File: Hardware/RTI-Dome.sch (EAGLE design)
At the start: 48 parts, among them IC1 24AA128ST, IC2 74LVC244, IC3 FT232RL, IC4 74ABT244, X13 PN61729-S

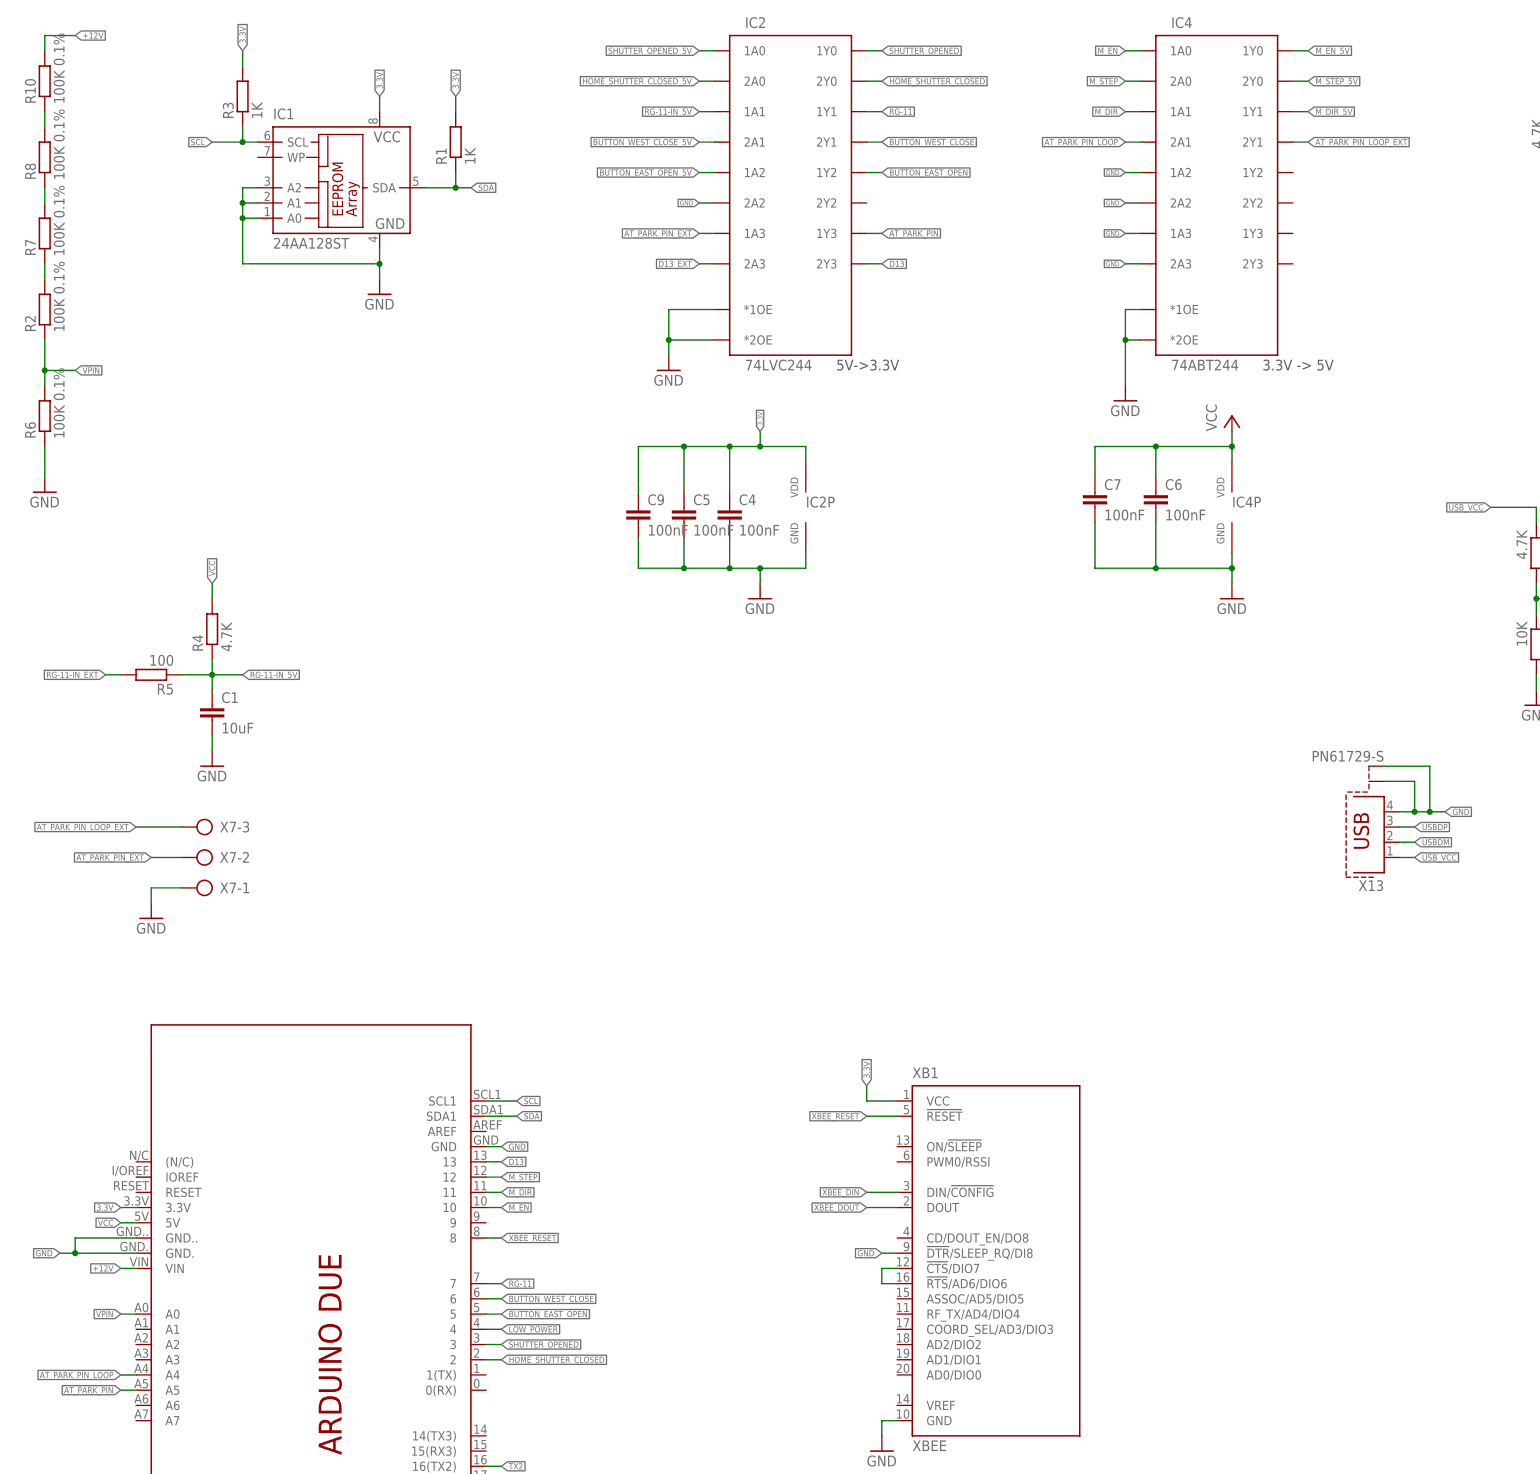
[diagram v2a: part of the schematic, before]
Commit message: Re-did the board with 74xx245 buffers instead of 244. Easier to route. Added a png to enable/disable the input buffer so that we can enable them after setting the interrupt and other things. It is disable on power up via a pull-up.
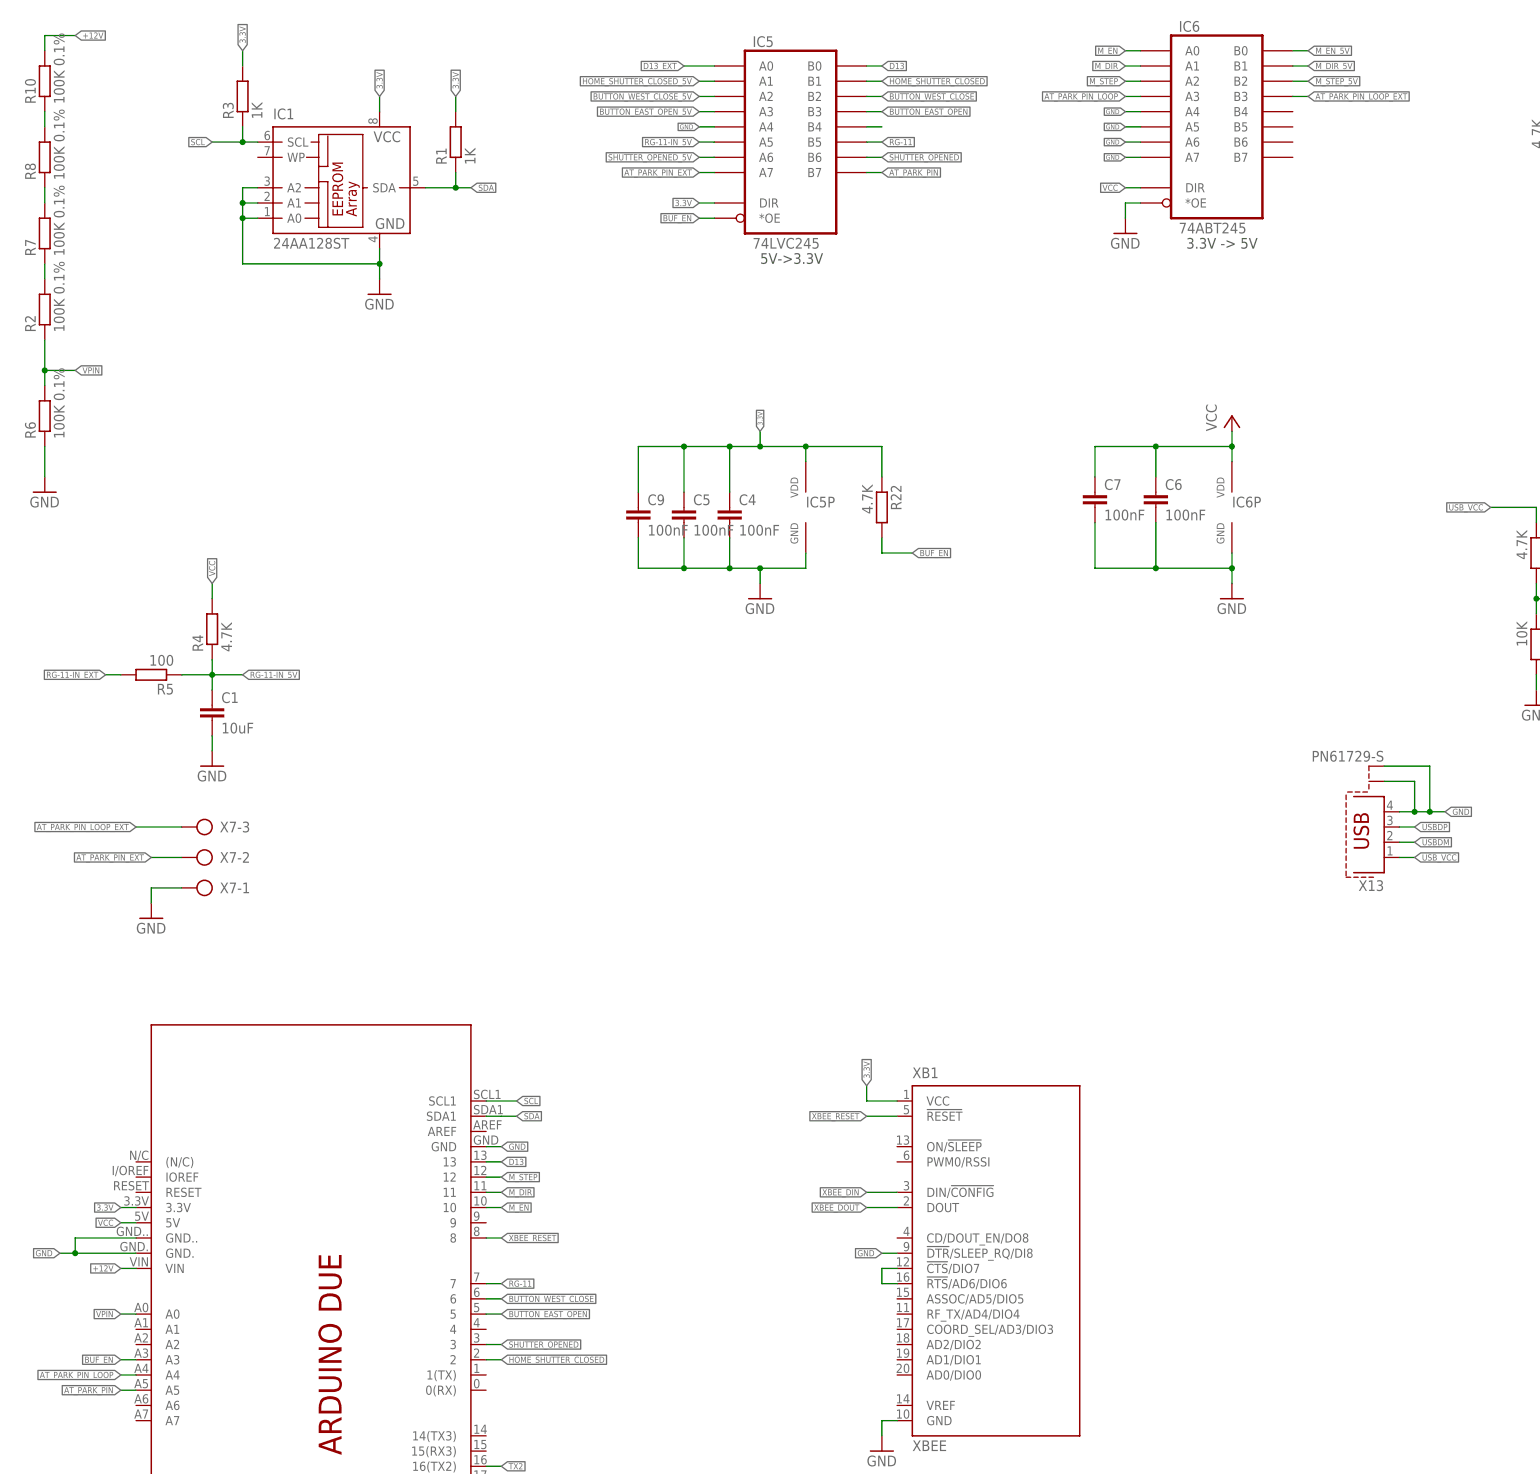
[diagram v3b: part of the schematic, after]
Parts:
- removed IC2: 74LVC244, rti:74LVC244
- removed IC4: 74ABT244, rti:74LVC244
- added IC5: 74LVC245, rti:74LVC245
- added IC6: 74ABT245, rti:74LVC245
- added R22: 4.7K, rti:R-EU'0805'
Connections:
- removed net LOW_POWER: PCB1.4
- new net BUF_EN: IC5G$1.*OE, PCB1.A3, R22.2
- new net N$4: IC5G$1.B4
- net 3.3V: now also IC5G$1.DIR, IC5P.VDD, R22.1; no longer IC2P.VDD
- net AT_PARK_PIN: now also IC5G$1.B7; no longer IC2G$1.1Y3
- net AT_PARK_PIN_EXT: now also IC5G$1.A7; no longer IC2G$1.1A3
- net AT_PARK_PIN_LOOP: now also IC6G$1.A3; no longer IC4G$1.2A1
- net AT_PARK_PIN_LOOP_EXT: now also IC6G$1.B3; no longer IC4G$1.2Y1
- net BUTTON_EAST_OPEN: now also IC5G$1.B3; no longer IC2G$1.1Y2
- net BUTTON_EAST_OPEN_5V: now also IC5G$1.A3; no longer IC2G$1.1A2
- net BUTTON_WEST_CLOSE: now also IC5G$1.B2; no longer IC2G$1.2Y1
- net BUTTON_WEST_CLOSE_5V: now also IC5G$1.A2; no longer IC2G$1.2A1
- net D13: now also IC5G$1.B0; no longer IC2G$1.2Y3
- net D13_EXT: now also IC5G$1.A0; no longer IC2G$1.2A3
- net GND: now also IC5G$1.A4, IC5P.GND, IC6G$1.*OE, IC6G$1.A4, IC6G$1.A5, IC6G$1.A6, IC6G$1.A7, IC6P.GND; no longer IC2G$1.*1OE, IC2G$1.*2OE, IC2G$1.2A2, IC2P.GND, IC4G$1.*1OE, IC4G$1.*2OE, IC4G$1.1A2, IC4G$1.1A3, IC4G$1.2A2, IC4G$1.2A3, IC4P.GND
- net HOME_SHUTTER_CLOSED: now also IC5G$1.B1; no longer IC2G$1.2Y0
- net HOME_SHUTTER_CLOSED_5V: now also IC5G$1.A1; no longer IC2G$1.2A0
- net M_DIR: now also IC6G$1.A1; no longer IC4G$1.1A1
- net M_DIR_5V: now also IC6G$1.B1; no longer IC4G$1.1Y1
- net M_EN: now also IC6G$1.A0; no longer IC4G$1.1A0
- net M_EN_5V: now also IC6G$1.B0; no longer IC4G$1.1Y0
- net M_STEP: now also IC6G$1.A2; no longer IC4G$1.2A0
- net M_STEP_5V: now also IC6G$1.B2; no longer IC4G$1.2Y0
- net RG-11: now also IC5G$1.B5; no longer IC2G$1.1Y1
- net RG-11-IN_5V: now also IC5G$1.A5; no longer IC2G$1.1A1
- net SHUTTER_OPENED: now also IC5G$1.B6; no longer IC2G$1.1Y0
- net SHUTTER_OPENED_5V: now also IC5G$1.A6; no longer IC2G$1.1A0
- net VCC: now also IC6G$1.DIR, IC6P.VDD; no longer IC4P.VDD
